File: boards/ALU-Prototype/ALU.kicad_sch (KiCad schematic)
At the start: 4 parts

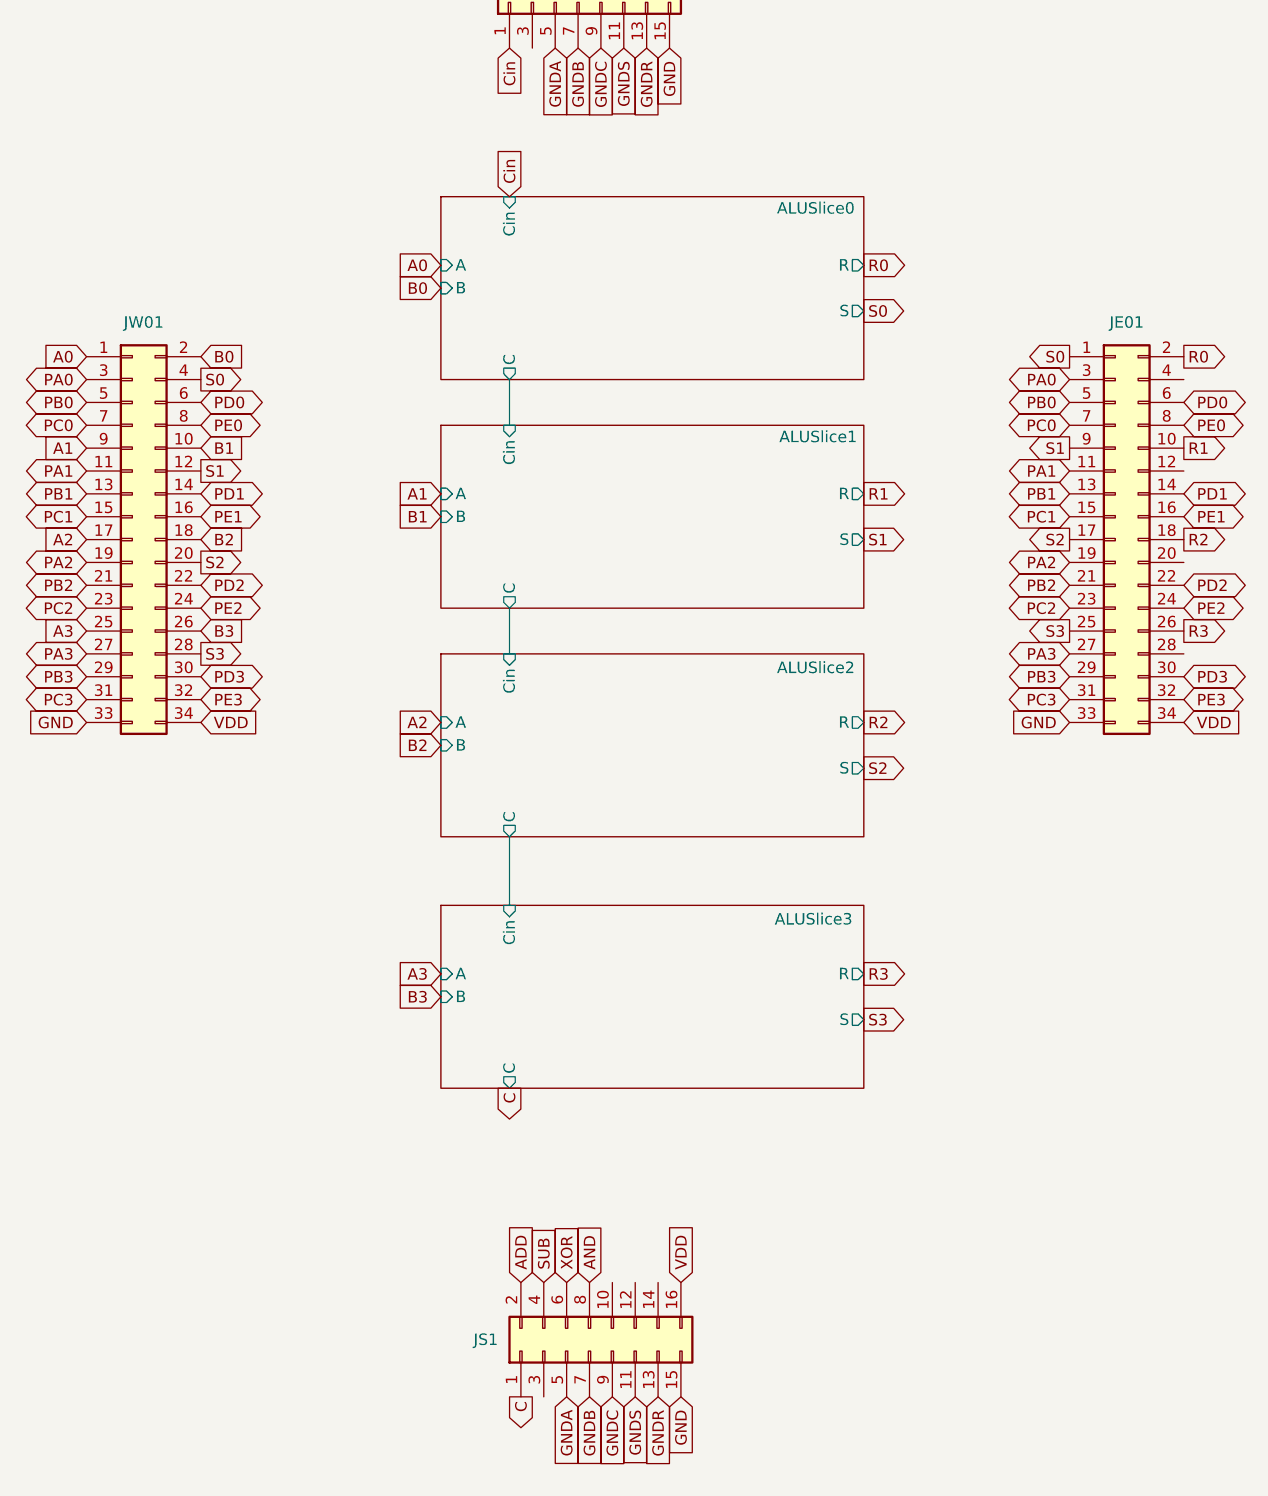
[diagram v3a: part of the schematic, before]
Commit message: Schematic for 8-bit ALU
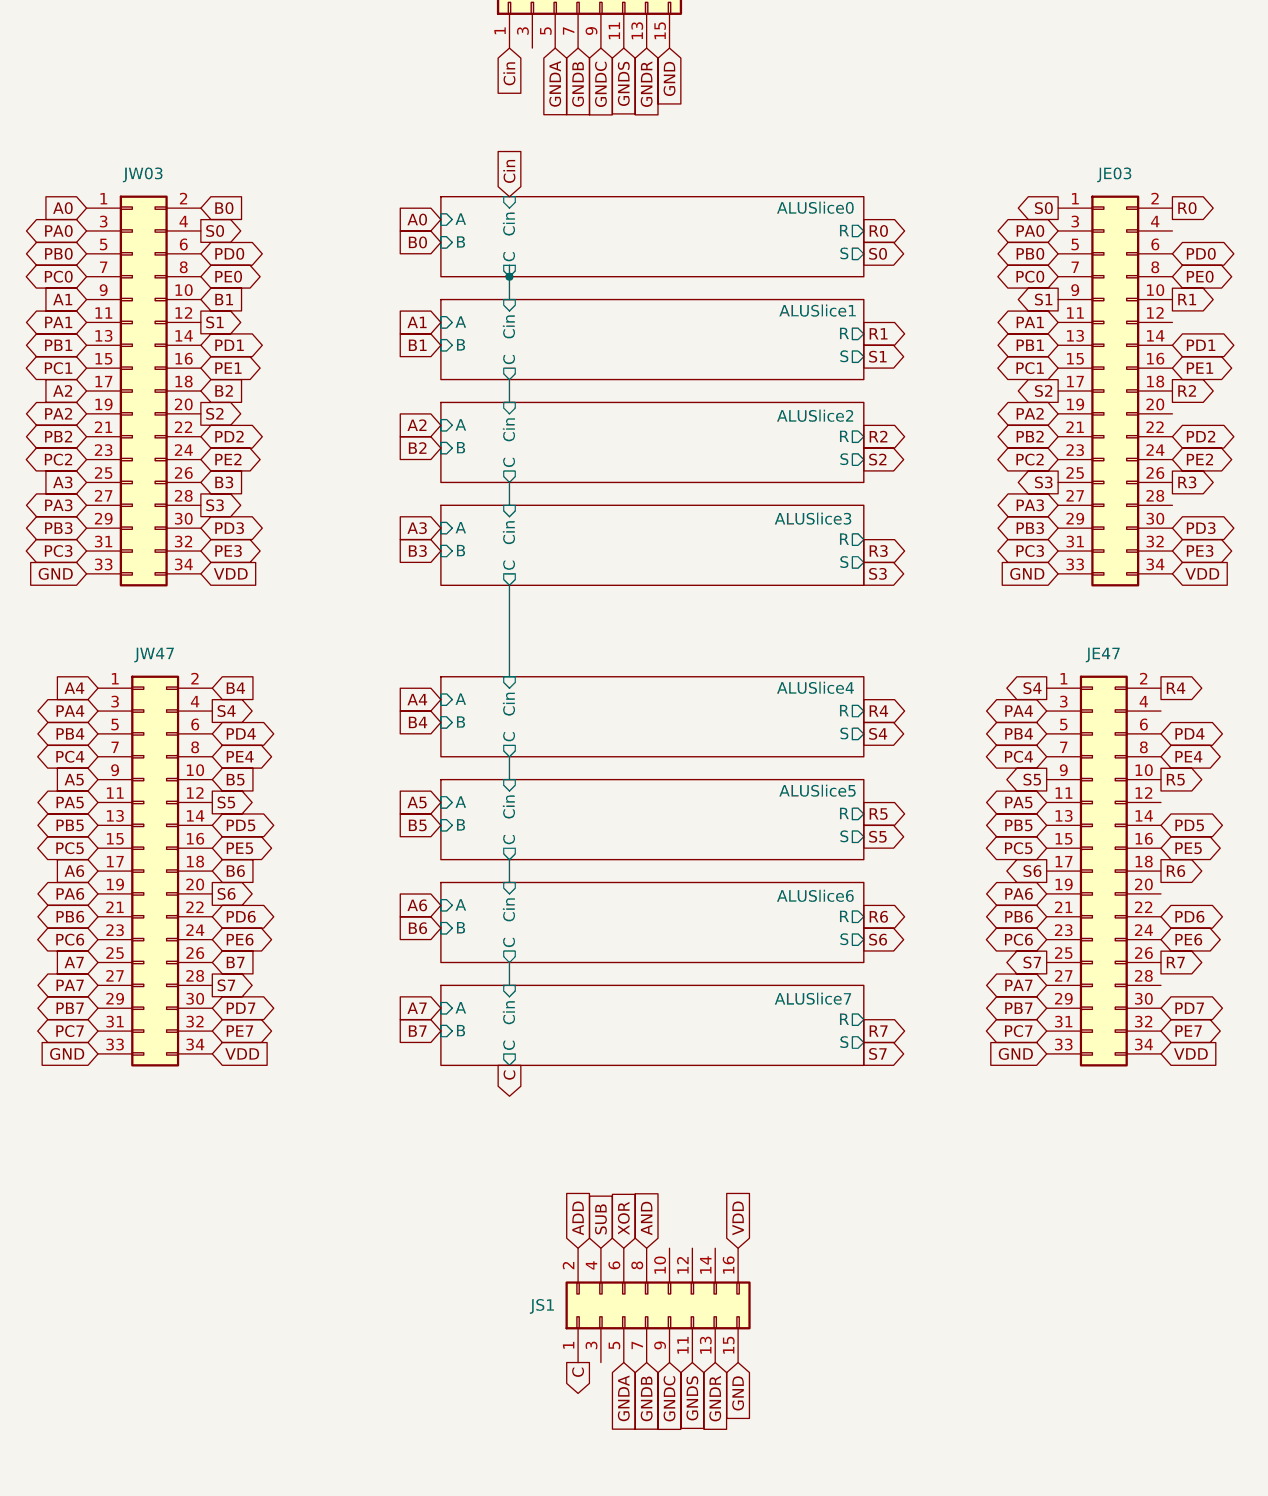
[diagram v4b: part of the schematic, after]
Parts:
- added JE47, JW47: ~, Connector_PinHeader_2.54mm:PinHeader_2x17_P2.54mm_Vertical, symbol Connector_Generic:Conn_02x17_Odd_Even
- renumbered JE01 to JE03, JW01 to JW03
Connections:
- net GND: now also JE47.33 (Pin_33), JW47.33 (Pin_33)
- net VDD: now also JE47.34 (Pin_34), JW47.34 (Pin_34)
- new net A4: JW47.1 (Pin_1)
- new net A5: JW47.9 (Pin_9)
- new net A6: JW47.17 (Pin_17)
- new net A7: JW47.25 (Pin_25)
- new net B4: JW47.2 (Pin_2)
- new net B5: JW47.10 (Pin_10)
- new net B6: JW47.18 (Pin_18)
- new net B7: JW47.26 (Pin_26)
- new net PA4: JE47.3 (Pin_3), JW47.3 (Pin_3)
- new net PA5: JE47.11 (Pin_11), JW47.11 (Pin_11)
- new net PA6: JE47.19 (Pin_19), JW47.19 (Pin_19)
- new net PA7: JE47.27 (Pin_27), JW47.27 (Pin_27)
- new net PB4: JE47.5 (Pin_5), JW47.5 (Pin_5)
- new net PB5: JE47.13 (Pin_13), JW47.13 (Pin_13)
- new net PB6: JE47.21 (Pin_21), JW47.21 (Pin_21)
- new net PB7: JE47.29 (Pin_29), JW47.29 (Pin_29)
- new net PC4: JE47.7 (Pin_7), JW47.7 (Pin_7)
- new net PC5: JE47.15 (Pin_15), JW47.15 (Pin_15)
- new net PC6: JE47.23 (Pin_23), JW47.23 (Pin_23)
- new net PC7: JE47.31 (Pin_31), JW47.31 (Pin_31)
- new net PD4: JE47.6 (Pin_6), JW47.6 (Pin_6)
- new net PD5: JE47.14 (Pin_14), JW47.14 (Pin_14)
- new net PD6: JE47.22 (Pin_22), JW47.22 (Pin_22)
- new net PD7: JE47.30 (Pin_30), JW47.30 (Pin_30)
- new net PE4: JE47.8 (Pin_8), JW47.8 (Pin_8)
- new net PE5: JE47.16 (Pin_16), JW47.16 (Pin_16)
- new net PE6: JE47.24 (Pin_24), JW47.24 (Pin_24)
- new net PE7: JE47.32 (Pin_32), JW47.32 (Pin_32)
- new net R4: JE47.2 (Pin_2)
- new net R5: JE47.10 (Pin_10)
- new net R6: JE47.18 (Pin_18)
- new net R7: JE47.26 (Pin_26)
- new net S4: JE47.1 (Pin_1), JW47.4 (Pin_4)
- new net S5: JE47.9 (Pin_9), JW47.12 (Pin_12)
- new net S6: JE47.17 (Pin_17), JW47.20 (Pin_20)
- new net S7: JE47.25 (Pin_25), JW47.28 (Pin_28)
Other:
- added sheet ALUSlice4 (ALUSlice.kicad_sch)
- added sheet ALUSlice5 (ALUSlice.kicad_sch)
- added sheet ALUSlice6 (ALUSlice.kicad_sch)
- added sheet ALUSlice7 (ALUSlice.kicad_sch)
- moved on the sheet: JE03, JS1, JW03

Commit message: 8-bit PCB, P1 version
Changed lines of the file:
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@@
 	(generator_version "9.0")
 	(paper "A4")
-	(junction
-		(at 128.27 58.42)
-		(diameter 0)
-		(color 0 0 0 0)
-	)
 	(wire
 		(pts
@@
 		)
 	)
-	(wire
-		(pts
-			(xy 128.27 57.15) (xy 128.27 58.42)
-		)
-		(stroke
-			(width 0)
-			(type default)
-		)
-	)
 	(global_label "PB7"
 		(shape bidirectional)
@@
 	(global_label "S3"
 		(shape output)
-		(at 167.64 91.44 0)
+		(at 167.64 90.17 0)
 		(fields_autoplaced yes)
 		(effects
@@
 		)
 		(property "Intersheetrefs" "${INTERSHEET_REFS}"
-			(at 162.2358 91.44 0)
+			(at 162.2358 90.17 0)
 			(effects
 				(font
@@
 	(global_label "R3"
 		(shape output)
-		(at 167.64 88.9 0)
+		(at 167.64 87.63 0)
 		(fields_autoplaced yes)
 		(effects
@@
 		)
 		(property "Intersheetrefs" "${INTERSHEET_REFS}"
-			(at 173.1047 88.9 0)
+			(at 173.1047 87.63 0)
 			(effects
 				(font
@@
 	(global_label "S7"
 		(shape output)
-		(at 167.64 144.78 0)
+		(at 167.64 143.51 0)
 		(fields_autoplaced yes)
 		(effects
@@
 		)
 		(property "Intersheetrefs" "${INTERSHEET_REFS}"
-			(at 173.0442 144.78 0)
+			(at 173.0442 143.51 0)
 			(effects
 				(font
@@
 	(global_label "R7"
 		(shape output)
-		(at 167.64 142.24 0)
+		(at 167.64 140.97 0)
 		(fields_autoplaced yes)
 		(effects
@@
 		)
 		(property "Intersheetrefs" "${INTERSHEET_REFS}"
-			(at 173.1047 142.24 0)
+			(at 173.1047 140.97 0)
 			(effects
 				(font

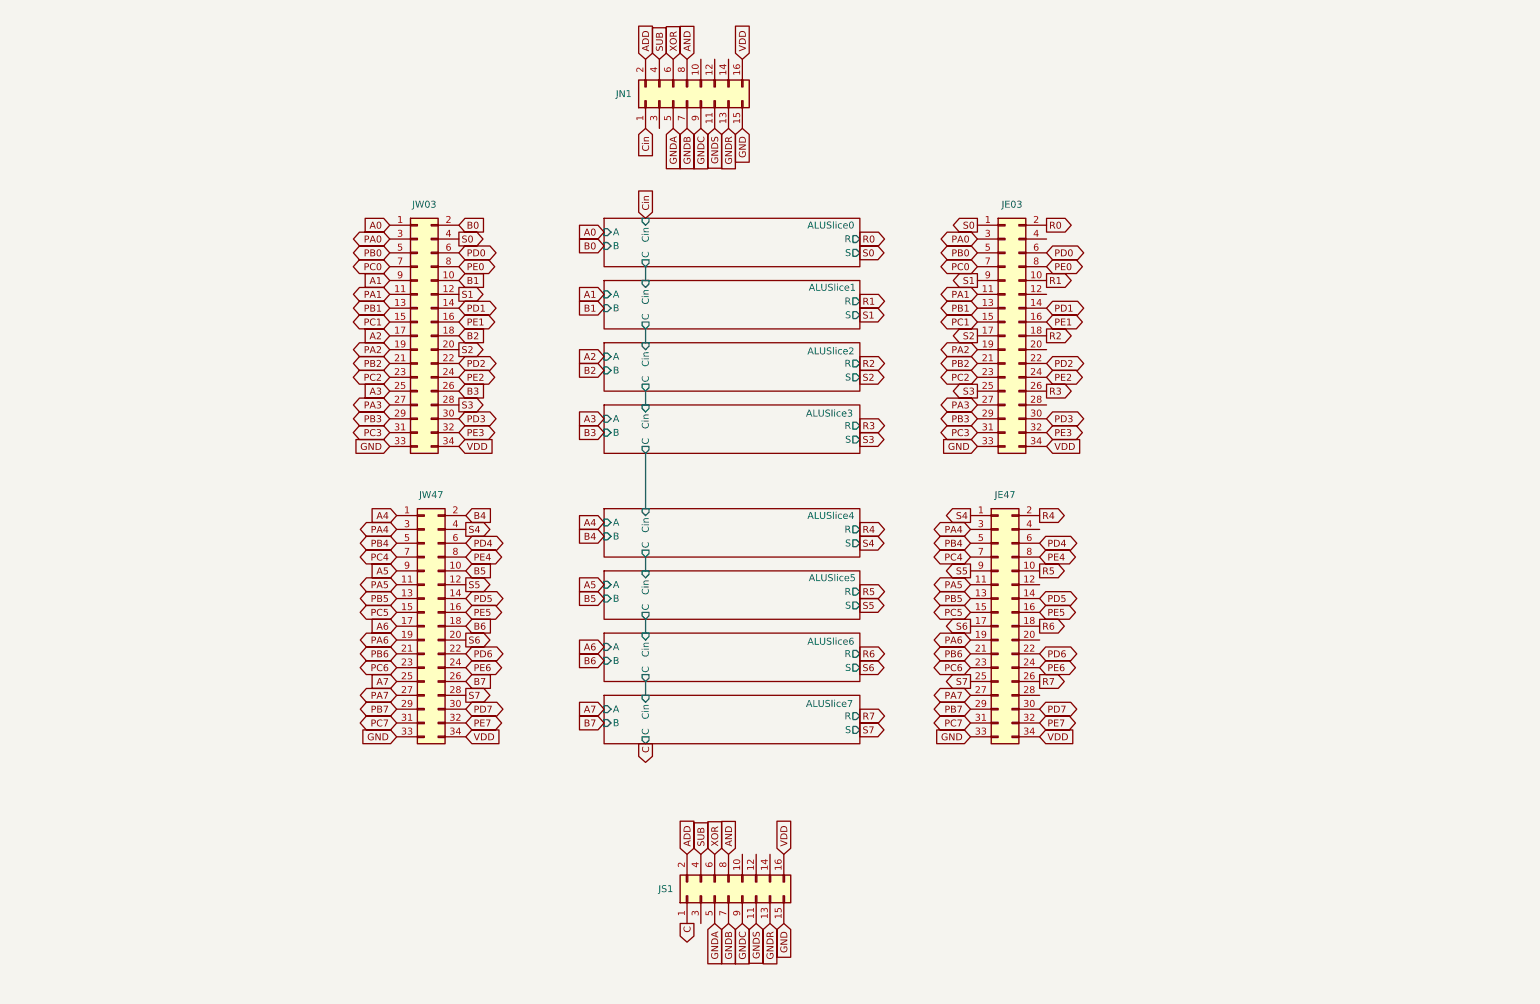
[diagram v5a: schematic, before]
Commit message: schematic with solder jumpers for S31/C31
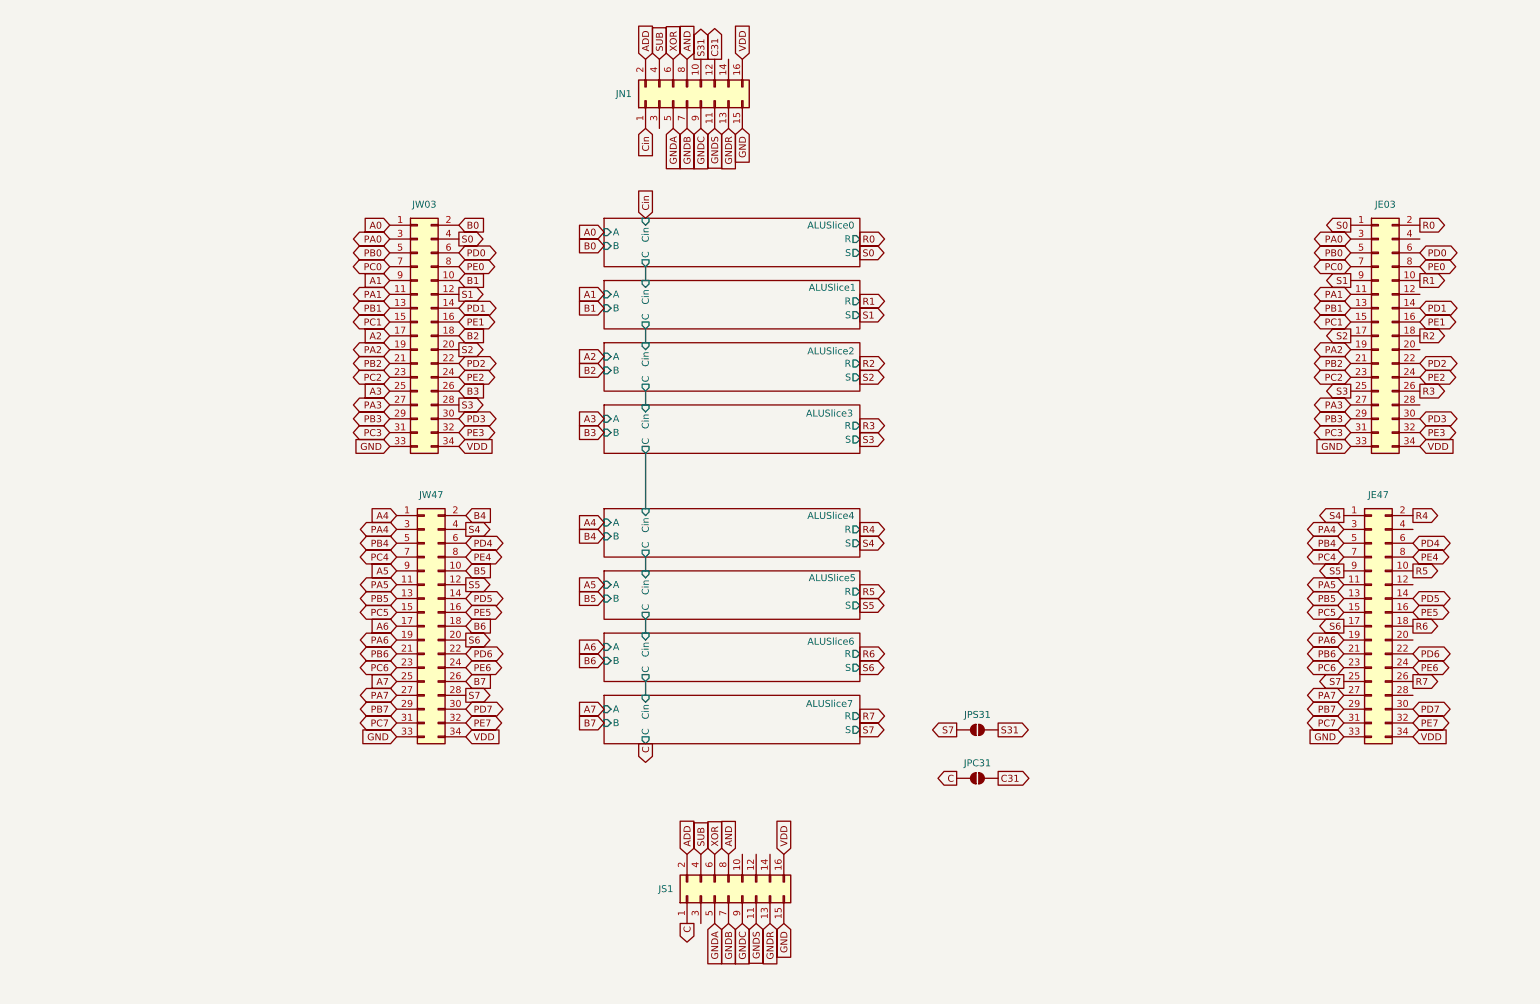
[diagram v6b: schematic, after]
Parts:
- added JPC31, JPS31: SolderJumper_2_Open, symbol Jumper:SolderJumper_2_Open
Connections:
- net C: now also JPC31.1 (A)
- net S7: now also JPS31.1 (A)
- net S31: now reaches JN1.10 (Pin_10)
- net S31: now also JPS31.2 (B)
- net C31: now reaches JN1.12 (Pin_12)
- net C31: now also JPC31.2 (B)
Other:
- moved on the sheet: JE03, JE47

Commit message: Schematic with Equality circuit
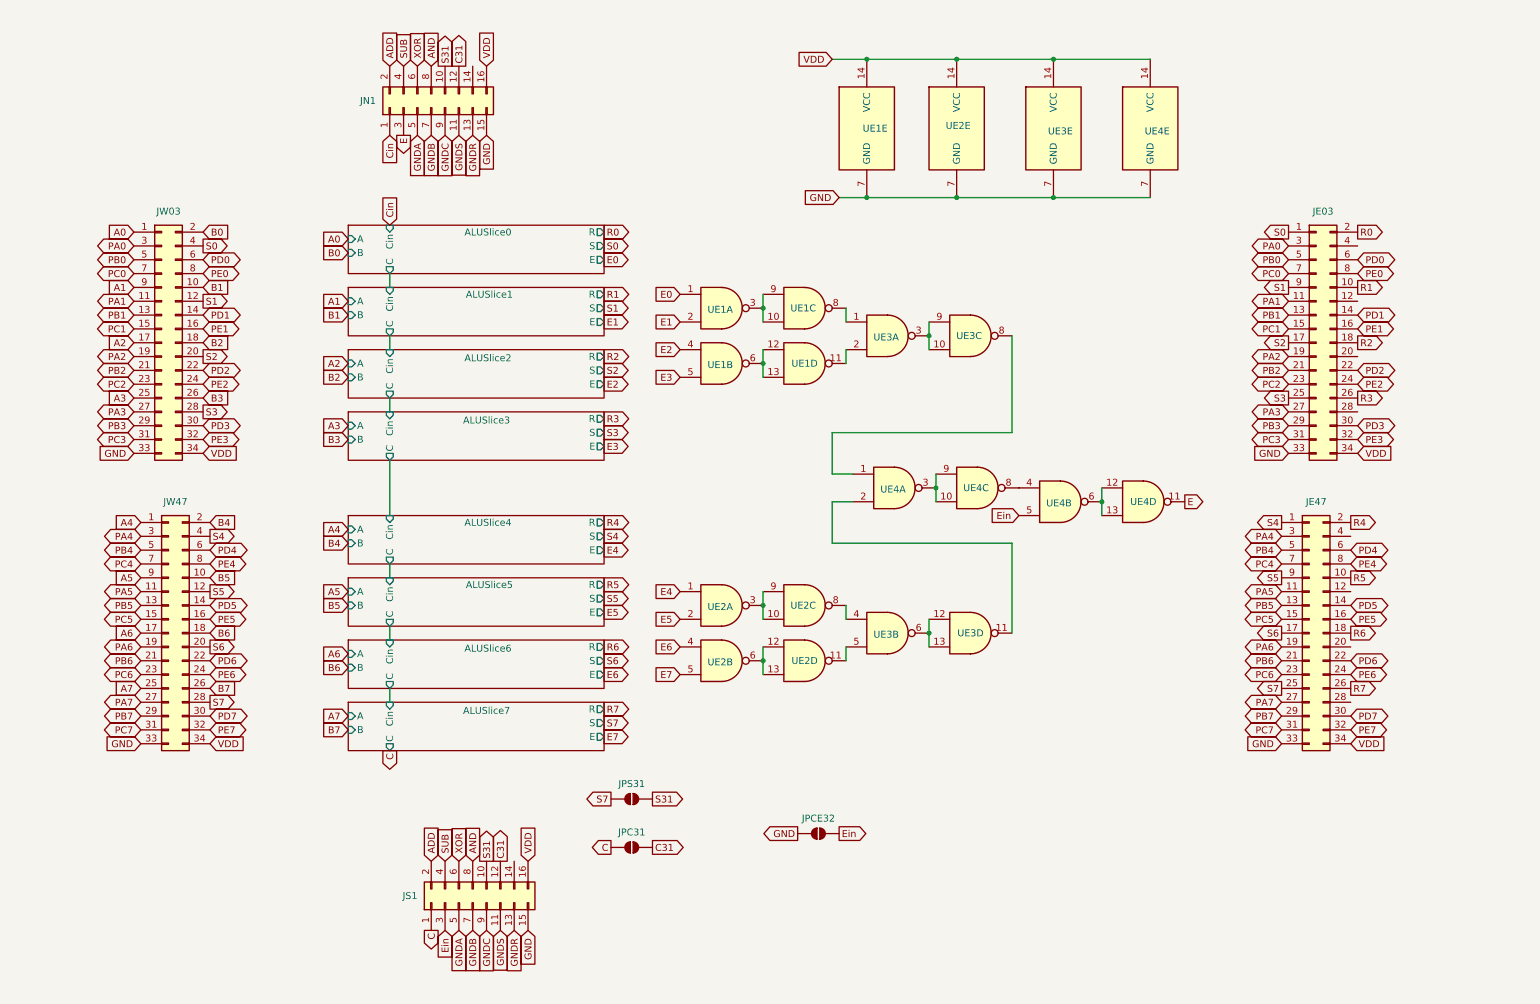
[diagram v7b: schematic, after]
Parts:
- added JPCE32: SolderJumper_2_Open, Jumper:SolderJumper-2_P1.3mm_Open_Pad1.0x1.5mm, symbol Jumper:SolderJumper_2_Open
- added UE1, UE2, UE3, UE4: ~, Package_SO:TSSOP-14_4.4x5mm_P0.65mm, symbol 74xx:7400
- JPC31, JPS31: footprint (none) -> Jumper:SolderJumper-2_P1.3mm_Open_Pad1.0x1.5mm
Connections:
- net C31: now also JS1.12 (Pin_12)
- net GND: now also JPCE32.1 (A), UE1.7 (GND), UE2.7 (GND), UE3.7 (GND), UE4.7 (GND)
- net S31: now also JS1.10 (Pin_10)
- net VDD: now also UE1.14 (VCC), UE2.14 (VCC), UE3.14 (VCC), UE4.14 (VCC)
- net E: now reaches JN1.3 (Pin_3)
- net E: now also UE4.11
- net Ein: now reaches JS1.3 (Pin_3)
- net Ein: now also JPCE32.2 (B), UE4.5
- new net: UE1.8, UE3.1
- new net: UE1.11, UE3.2
- new net: UE3.10, UE3.3, UE3.9
- new net: UE4.12, UE4.13, UE4.6
- new net: UE2.10, UE2.3, UE2.9
- new net: UE1.12, UE1.13, UE1.6
- new net: UE2.12, UE2.13, UE2.6
- new net: UE3.8, UE4.1
- new net: UE3.11, UE4.2
- new net: UE4.10, UE4.3, UE4.9
- new net: UE3.12, UE3.13, UE3.6
- new net: UE2.8, UE3.4
- new net: UE2.11, UE3.5
- new net: UE4.4, UE4.8
- new net: UE1.10, UE1.3, UE1.9
- new net E0: UE1.1
- new net E1: UE1.2
- new net E2: UE1.4
- new net E3: UE1.5
- new net E4: UE2.1
- new net E5: UE2.2
- new net E6: UE2.4
- new net E7: UE2.5
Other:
- sheet ALUSlice0 ports: added E; removed none
- sheet ALUSlice1 ports: added E; removed none
- sheet ALUSlice2 ports: added E; removed none
- sheet ALUSlice3 ports: added E; removed none
- sheet ALUSlice4 ports: added E; removed none
- sheet ALUSlice5 ports: added E; removed none
- sheet ALUSlice6 ports: added E; removed none
- sheet ALUSlice7 ports: added E; removed none
- moved on the sheet: JE03, JE47, JN1, JPC31, JPS31, JS1, JW03, JW47
